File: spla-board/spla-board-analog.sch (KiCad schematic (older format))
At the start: 99 parts, among them J13 J_ANALOG, J14 J_AREF, J8 J_AREF_AMP, U51 ADC1173, U52 ADC1173, U53 ADC1173, U61 LMH6611, U62 LMH6611, U63 LMH6611, U74 LMH6611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

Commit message: bom: Add manufacturers.
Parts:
- BOM10, BOM11, BOM4, BOM5, BOM6, BOM7, BOM8, BOM9, J13, J14, J8: Manufacturer (none) -> Sullins Connector Solutions
- TP3, TP4: Manufacturer (none) -> N/A
- U51, U52, U53, U61, U62, U63, U74, U75, U76: Manufacturer (none) -> Texas Instruments
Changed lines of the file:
@@
 F 4 "S2011EC-40-ND" H 2100 8850 50  0001 C CNN "Digikey"
 F 5 "PRPC040DAAN-RC" H 2100 8850 50  0001 C CNN "Manufacturer Id"
+F 6 "Sullins Connector Solutions" H 2100 8850 50  0001 C CNN "Manufacturer"
 	1    2100 8850
 	1    0    0    -1
@@
 F 4 "S2011EC-40-ND" H 6250 3000 50  0001 C CNN "Digikey"
 F 5 "PRPC040DAAN-RC" H 6250 3000 50  0001 C CNN "Manufacturer Id"
+F 6 "Sullins Connector Solutions" H 6250 3000 50  0001 C CNN "Manufacturer"
 	1    6250 3000
 	1    0    0    -1
@@
 F 4 "N/A" H 6200 8700 50  0001 C CNN "Digikey"
 F 5 "N/A" H 6200 8700 50  0001 C CNN "Manufacturer Id"
+F 6 "N/A" H 6200 8700 50  0001 C CNN "Manufacturer"
 	1    6200 8700
 	1    0    0    -1
@@
 F 4 "N/A" H 6200 8900 50  0001 C CNN "Digikey"
 F 5 "N/A" H 6200 8900 50  0001 C CNN "Manufacturer Id"
+F 6 "N/A" H 6200 8900 50  0001 C CNN "Manufacturer"
 	1    6200 8900
 	-1   0    0    1
@@
 F 4 "296-35234-1-ND" H 14300 2550 50  0001 C CNN "Digikey"
 F 5 "ADC1173CIMTCX/NOPB" H 14300 2550 50  0001 C CNN "Manufacturer Id"
+F 6 "Texas Instruments" H 14300 2550 50  0001 C CNN "Manufacturer"
 	1    14300 2550
 	1    0    0    -1
@@
 F 4 "296-35234-1-ND" H 14300 8650 50  0001 C CNN "Digikey"
 F 5 "ADC1173CIMTCX/NOPB" H 14300 8650 50  0001 C CNN "Manufacturer Id"
+F 6 "Texas Instruments" H 14300 8650 50  0001 C CNN "Manufacturer"
 	1    14300 8650
 	1    0    0    -1
@@
 F 4 "296-35234-1-ND" H 14300 5600 50  0001 C CNN "Digikey"
 F 5 "ADC1173CIMTCX/NOPB" H 14300 5600 50  0001 C CNN "Manufacturer Id"
+F 6 "Texas Instruments" H 14300 5600 50  0001 C CNN "Manufacturer"
 	1    14300 5600
 	1    0    0    -1
@@
 F 4 "296-41441-1-ND" H 9550 8250 50  0001 C CNN "Digikey"
 F 5 "LMH6611MK/NOPB" H 9550 8250 50  0001 C CNN "Manufacturer Id"
+F 6 "Texas Instruments" H 9550 8250 50  0001 C CNN "Manufacturer"
 	1    9550 8250
 	1    0    0    -1
@@
 F 4 "296-41441-1-ND" H 9550 2150 50  0001 C CNN "Digikey"
 F 5 "LMH6611MK/NOPB" H 9550 2150 50  0001 C CNN "Manufacturer Id"
+F 6 "Texas Instruments" H 9550 2150 50  0001 C CNN "Manufacturer"
 	1    9550 2150
 	1    0    0    -1
@@
 F 4 "296-41441-1-ND" H 9550 5200 50  0001 C CNN "Digikey"
 F 5 "LMH6611MK/NOPB" H 9550 5200 50  0001 C CNN "Manufacturer Id"
+F 6 "Texas Instruments" H 9550 5200 50  0001 C CNN "Manufacturer"
 	1    9550 5200
 	1    0    0    -1
@@
 F 4 "296-41441-1-ND" H 4300 7350 50  0001 C CNN "Digikey"
 F 5 "LMH6611MK/NOPB" H 4300 7350 50  0001 C CNN "Manufacturer Id"
+F 6 "Texas Instruments" H 4300 7350 50  0001 C CNN "Manufacturer"
 	1    4300 7350
 	1    0    0    -1
@@
 F 4 "S2011EC-40-ND" H 5800 8800 50  0001 C CNN "Digikey"
 F 5 "PRPC040DAAN-RC" H 5800 8800 50  0001 C CNN "Manufacturer Id"
+F 6 "Sullins Connector Solutions" H 5800 8800 50  0001 C CNN "Manufacturer"
 	1    5800 8800
 	1    0    0    -1
@@
 F 4 "296-41441-1-ND" H 4300 9900 50  0001 C CNN "Digikey"
 F 5 "LMH6611MK/NOPB" H 4300 9900 50  0001 C CNN "Manufacturer Id"
+F 6 "Texas Instruments" H 4300 9900 50  0001 C CNN "Manufacturer"
 	1    4300 9900
 	1    0    0    -1
@@
 F 4 "296-40673-1-ND" H 2000 6900 50  0001 C CNN "Digikey"
 F 5 "TLV73333PDBVR" H 2000 6900 50  0001 C CNN "Manufacturer Id"
+F 6 "Texas Instruments" H 2000 6900 50  0001 C CNN "Manufacturer"
 	1    2000 6900
 	1    0    0    -1
@@
 F 4 "S9337-ND" H 1950 9850 50  0001 C CNN "Digikey"
 F 5 "QPC02SXGN-RC" H 1950 9850 50  0001 C CNN "Manufacturer Id"
+F 6 "Sullins Connector Solutions" H 1950 9850 50  0001 C CNN "Manufacturer"
 	1    1950 9850
 	1    0    0    -1
@@
 F 4 "S9337-ND" H 1950 10100 50  0001 C CNN "Digikey"
 F 5 "QPC02SXGN-RC" H 1950 10100 50  0001 C CNN "Manufacturer Id"
+F 6 "Sullins Connector Solutions" H 1950 10100 50  0001 C CNN "Manufacturer"
 	1    1950 10100
 	1    0    0    -1
@@
 F 4 "S9337-ND" H 1950 10350 50  0001 C CNN "Digikey"
 F 5 "QPC02SXGN-RC" H 1950 10350 50  0001 C CNN "Manufacturer Id"
+F 6 "Sullins Connector Solutions" H 1950 10350 50  0001 C CNN "Manufacturer"
 	1    1950 10350
 	1    0    0    -1
@@
 F 4 "S9337-ND" H 5850 9300 50  0001 C CNN "Digikey"
 F 5 "QPC02SXGN-RC" H 5850 9300 50  0001 C CNN "Manufacturer Id"
+F 6 "Sullins Connector Solutions" H 5850 9300 50  0001 C CNN "Manufacturer"
 	1    5850 9300
 	1    0    0    -1
@@
 F 4 "S9337-ND" H 5850 9550 50  0001 C CNN "Digikey"
 F 5 "QPC02SXGN-RC" H 5850 9550 50  0001 C CNN "Manufacturer Id"
+F 6 "Sullins Connector Solutions" H 5850 9550 50  0001 C CNN "Manufacturer"
 	1    5850 9550
 	1    0    0    -1
@@
 F 4 "S9337-ND" H 6100 3600 50  0001 C CNN "Digikey"
 F 5 "QPC02SXGN-RC" H 6100 3600 50  0001 C CNN "Manufacturer Id"
+F 6 "Sullins Connector Solutions" H 6100 3600 50  0001 C CNN "Manufacturer"
 	1    6100 3600
 	1    0    0    -1
@@
 F 4 "S9337-ND" H 6100 3850 50  0001 C CNN "Digikey"
 F 5 "QPC02SXGN-RC" H 6100 3850 50  0001 C CNN "Manufacturer Id"
+F 6 "Sullins Connector Solutions" H 6100 3850 50  0001 C CNN "Manufacturer"
 	1    6100 3850
 	1    0    0    -1
@@
 F 4 "S9337-ND" H 6100 4100 50  0001 C CNN "Digikey"
 F 5 "QPC02SXGN-RC" H 6100 4100 50  0001 C CNN "Manufacturer Id"
+F 6 "Sullins Connector Solutions" H 6100 4100 50  0001 C CNN "Manufacturer"
 	1    6100 4100
 	1    0    0    -1

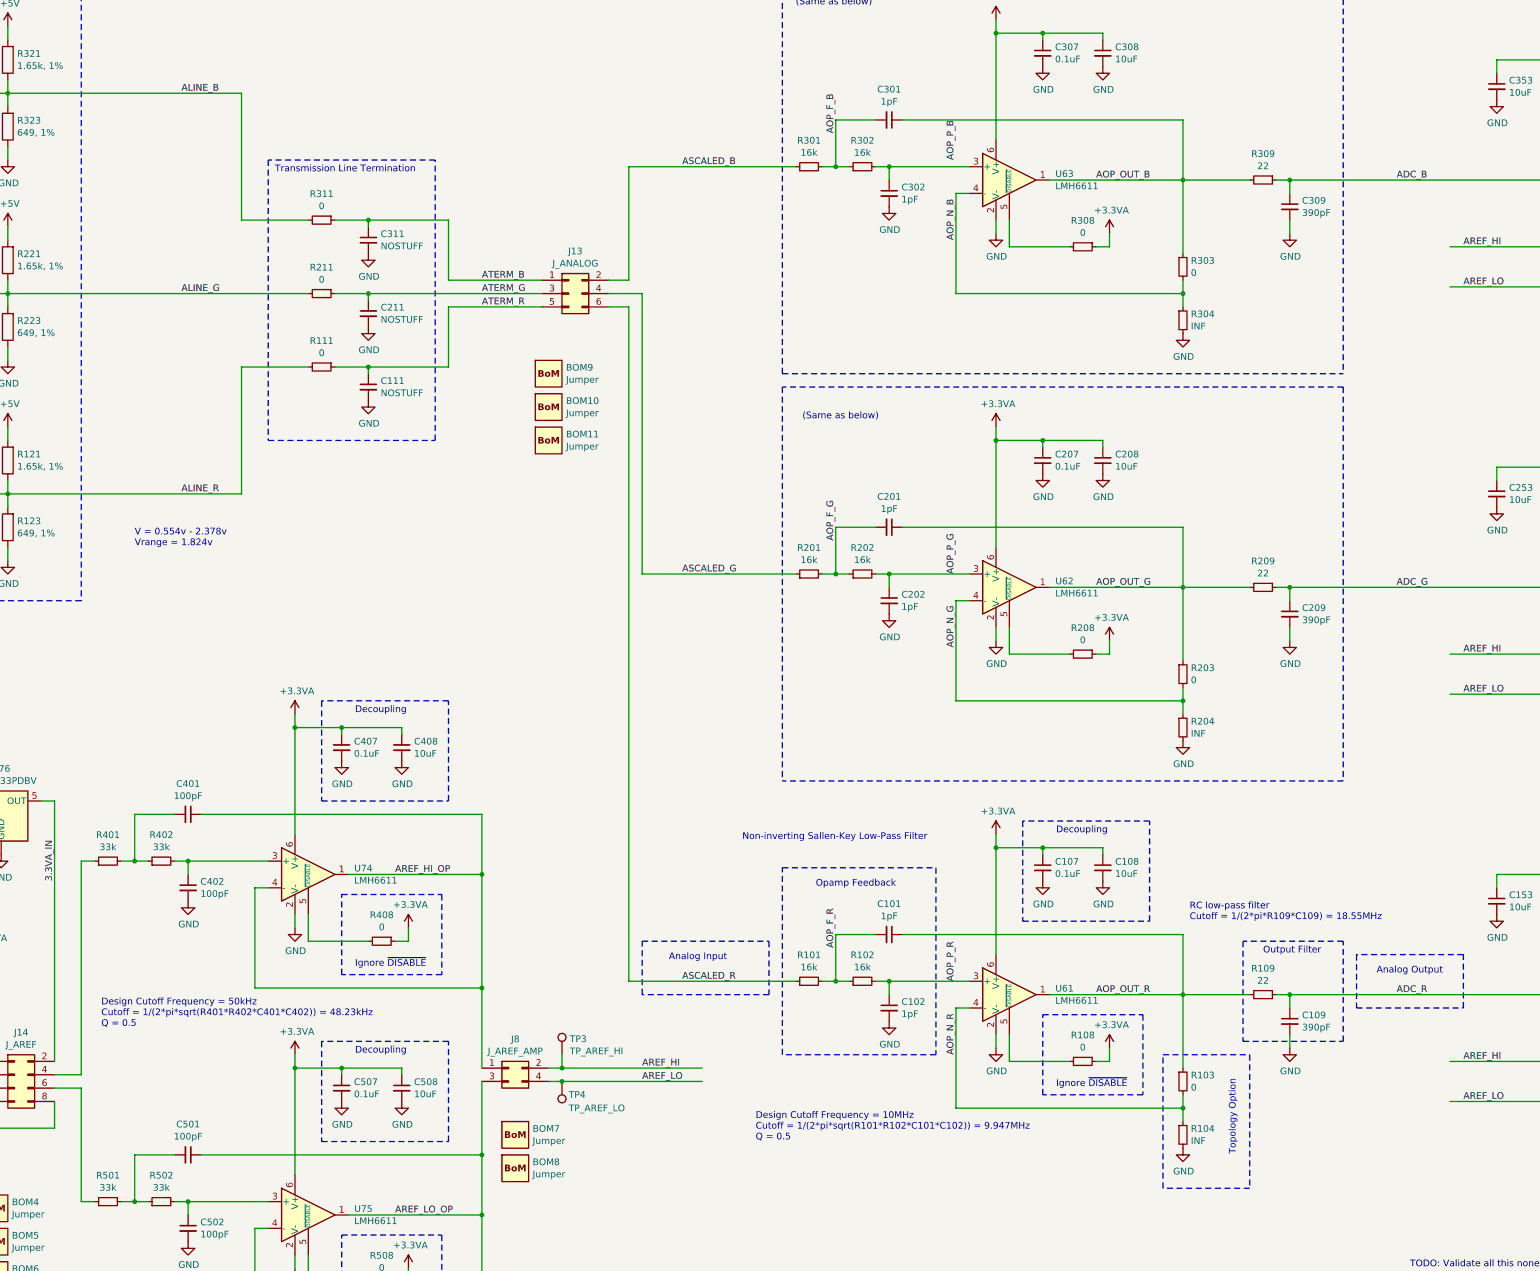
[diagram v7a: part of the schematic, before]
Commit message: schematic/pcb: Complete part selection of resistors and capacitors.  Omit filters in analog block for now; adjust PCB to suit.
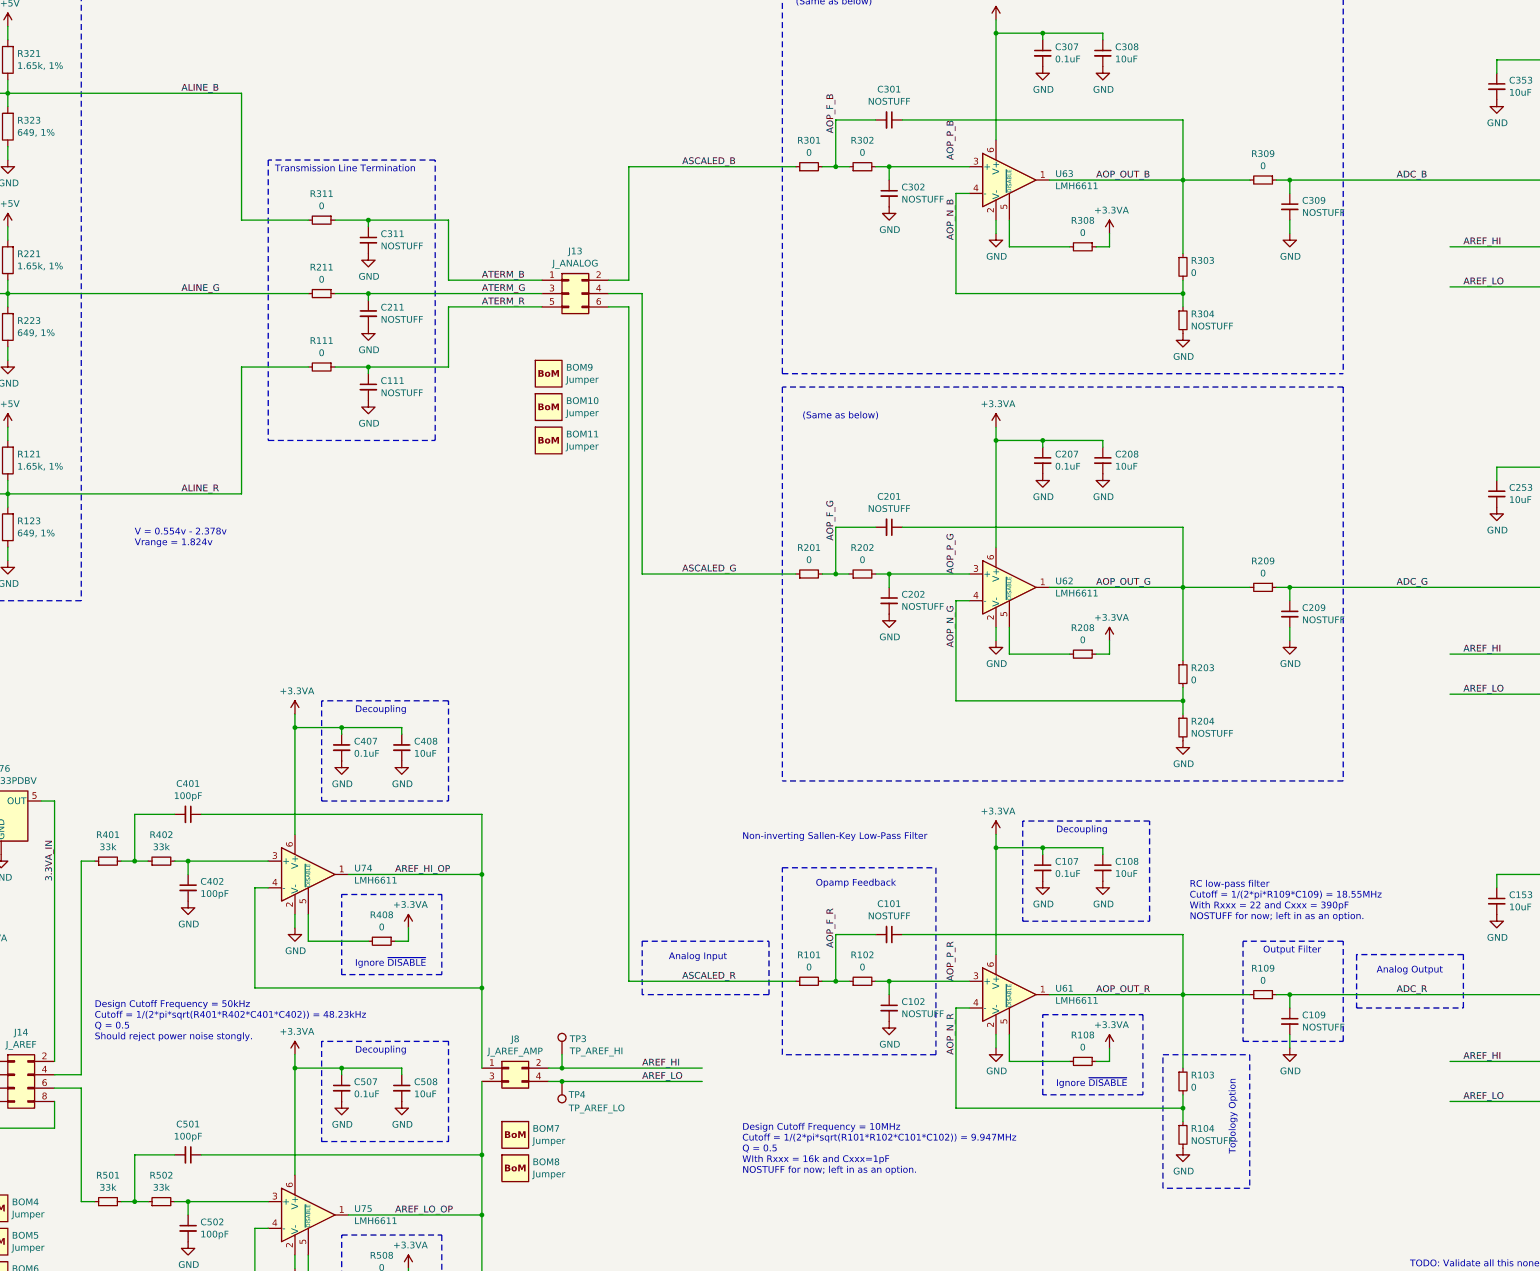
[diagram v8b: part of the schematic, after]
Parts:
- C101, C102, C201, C202, C301, C302: value 1pF -> NOSTUFF; Digikey (none) -> N/A; Manufacturer (none) -> N/A; Manufacturer Id (none) -> N/A
- C107, C151, C152, C207, C251, C252, C307, C351, C352, C407, C507: Digikey (none) -> 490-16477-1-ND; Manufacturer (none) -> Murata Electronics; Manufacturer Id (none) -> GCJ188R71E104KA12D
- C108, C153, C154, C208, C253, C254, C308, C353, C354, C408, C508: Digikey (none) -> 490-12538-1-ND; Manufacturer (none) -> Murata Electronics; Manufacturer Id (none) -> GRM188R60J106KE47D
- C109, C209, C309: value 390pF -> NOSTUFF; Digikey (none) -> N/A; Manufacturer (none) -> N/A; Manufacturer Id (none) -> N/A
- C111, C211, C311: Digikey (none) -> N/A; Manufacturer (none) -> N/A; Manufacturer Id (none) -> N/A
- C401, C402, C501, C502: Digikey (none) -> 490-4771-1-ND; Manufacturer (none) -> Murata Electronics; Manufacturer Id (none) -> GCM1885C2A101JA16D
- R101, R102, R201, R202, R301, R302: value 16k -> 0; Digikey (none) -> 2019-RK73Z1JTTDCT-ND; Manufacturer (none) -> KOA Speer Electronics Inc.; Manufacturer Id (none) -> RK73Z1JTTD
- R103, R108, R111, R203, R208, R211, R303, R308, R311, R408, R508: Digikey (none) -> 2019-RK73Z1JTTDCT-ND; Manufacturer (none) -> KOA Speer Electronics Inc.; Manufacturer Id (none) -> RK73Z1JTTD
- R104, R204, R304: value INF -> NOSTUFF; Digikey (none) -> N/A; Manufacturer (none) -> N/A; Manufacturer Id (none) -> N/A
- R109, R209, R309: value 22 -> 0; Digikey (none) -> 2019-RK73Z1JTTDCT-ND; Manufacturer (none) -> KOA Speer Electronics Inc.; Manufacturer Id (none) -> RK73Z1JTTD
- R121, R221, R321, R601: Digikey (none) -> RMCF0603FT1K65CT-ND; Manufacturer (none) -> Stackpole Electronics Inc; Manufacturer Id (none) -> RMCF0603FT1K65
- R122, R222, R322: Digikey (none) -> RMCF0603FT301RCT-ND; Manufacturer (none) -> Stackpole Electronics Inc; Manufacturer Id (none) -> RMCF0603FT301R
- R123, R223, R323: Digikey (none) -> RMCF0603FT649RCT-ND; Manufacturer (none) -> Stackpole Electronics Inc; Manufacturer Id (none) -> RMCF0603FT649R
- R401, R402, R501, R502: Digikey (none) -> RMCF0603JT33K0CT-ND; Manufacturer (none) -> Stackpole Electronics Inc; Manufacturer Id (none) -> RMCF0603JT33K0
- R602: Digikey (none) -> RMCF0603FT3K48CT-ND; Manufacturer (none) -> Stackpole Electronics Inc; Manufacturer Id (none) -> RMCF0603FT3K48
- R603: Digikey (none) -> RMCF0603FT1K00CT-ND; Manufacturer (none) -> Stackpole Electronics Inc; Manufacturer Id (none) -> RMCF0603FT1K00
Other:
- note added: "Design Cutoff Frequency = 10MHz\nCutoff = 1/(2*pi*sqrt(R101*R102*C101*C102)) = 9.947MHz\nQ = 0.5\nWIth Rxxx = 16k and Cxxx=1pF\nNOSTUFF for now; left in as an option."
- note added: "Design Cutoff Frequency = 50kHz\nCutoff = 1/(2*pi*sqrt(R401*R402*C401*C402)) = 48.23kHz\nQ = 0.5\nShould reject power noise stongly."
- note added: "RC low-pass filter\nCutoff = 1/(2*pi*R109*C109) = 18.55MHz\nWith Rxxx = 22 and Cxxx = 390pF\nNOSTUFF for now; left in as an option."
- note removed: "Design Cutoff Frequency = 10MHz\nCutoff = 1/(2*pi*sqrt(R101*R102*C101*C102)) = 9.947MHz\nQ = 0.5"
- note removed: "Design Cutoff Frequency = 50kHz\nCutoff = 1/(2*pi*sqrt(R401*R402*C401*C402)) = 48.23kHz\nQ = 0.5"
- note removed: "RC low-pass filter\nCutoff = 1/(2*pi*R109*C109) = 18.55MHz"
